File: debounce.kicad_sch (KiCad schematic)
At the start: 3 parts

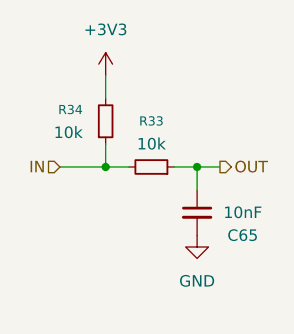
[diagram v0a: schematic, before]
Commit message: Add ultra thin buttons for ABXY
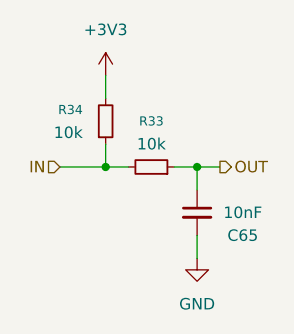
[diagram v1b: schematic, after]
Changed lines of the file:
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@@
+		)
+	)
+	(wire
+		(pts
+			(xy 134.62 111.76) (xy 134.62 109.22)
+		)
+		(stroke
+			(width 0)
+			(type default)
 		)
 	)
@@
 		(instances
 			(project "pedal"
+				(path "/e2443317-b83f-4e66-ac79-3186c6d613f3/08cc2b29-85b9-4aa1-81ca-cf2350ffd532/113d6eb1-d787-4bde-aeea-3b686f86928a"
+					(reference "R45")
+					(unit 1)
+				)
+				(path "/e2443317-b83f-4e66-ac79-3186c6d613f3/08cc2b29-85b9-4aa1-81ca-cf2350ffd532/24d60361-3370-44ad-88df-7f067c4a89f9"
+					(reference "R39")
+					(unit 1)
+				)
+				(path "/e2443317-b83f-4e66-ac79-3186c6d613f3/08cc2b29-85b9-4aa1-81ca-cf2350ffd532/30ff93b2-9c77-4a10-8b70-e2d38cabc23d"
+					(reference "R43")
+					(unit 1)
+				)
+				(path "/e2443317-b83f-4e66-ac79-3186c6d613f3/08cc2b29-85b9-4aa1-81ca-cf2350ffd532/7aa8d5d4-6cdc-47ee-9e8f-839e8028a7b9"
+					(reference "R49")
+					(unit 1)
+				)
+				(path "/e2443317-b83f-4e66-ac79-3186c6d613f3/08cc2b29-85b9-4aa1-81ca-cf2350ffd532/94183d09-d252-4744-b2a1-51f80f1daa54"
+					(reference "R41")
+					(unit 1)
+				)
+				(path "/e2443317-b83f-4e66-ac79-3186c6d613f3/08cc2b29-85b9-4aa1-81ca-cf2350ffd532/9e7ef8af-33b6-41d4-950e-29ca0f5a19bc"
+					(reference "R53")
+					(unit 1)
+				)
+				(path "/e2443317-b83f-4e66-ac79-3186c6d613f3/08cc2b29-85b9-4aa1-81ca-cf2350ffd532/d1f7dbf6-58aa-4f7e-8a98-9b343c116364"
+					(reference "R51")
+					(unit 1)
+				)
+				(path "/e2443317-b83f-4e66-ac79-3186c6d613f3/08cc2b29-85b9-4aa1-81ca-cf2350ffd532/e87d1f28-ed03-40a1-b111-b01404004c38"
+					(reference "R47")
+					(unit 1)
+				)
 				(path "/e2443317-b83f-4e66-ac79-3186c6d613f3/a1bbde72-fd3e-4fef-8e82-ce5db1c82ed5/4c22a4e9-863a-4116-bdb6-63d664a4292f"
 					(reference "R34")
@@
 		(instances
 			(project "pedal"
+				(path "/e2443317-b83f-4e66-ac79-3186c6d613f3/08cc2b29-85b9-4aa1-81ca-cf2350ffd532/113d6eb1-d787-4bde-aeea-3b686f86928a"
+					(reference "C71")
+					(unit 1)
+				)
+				(path "/e2443317-b83f-4e66-ac79-3186c6d613f3/08cc2b29-85b9-4aa1-81ca-cf2350ffd532/24d60361-3370-44ad-88df-7f067c4a89f9"
+					(reference "C68")
+					(unit 1)
+				)
+				(path "/e2443317-b83f-4e66-ac79-3186c6d613f3/08cc2b29-85b9-4aa1-81ca-cf2350ffd532/30ff93b2-9c77-4a10-8b70-e2d38cabc23d"
+					(reference "C70")
+					(unit 1)
+				)
+				(path "/e2443317-b83f-4e66-ac79-3186c6d613f3/08cc2b29-85b9-4aa1-81ca-cf2350ffd532/7aa8d5d4-6cdc-47ee-9e8f-839e8028a7b9"
+					(reference "C73")
+					(unit 1)
+				)
+				(path "/e2443317-b83f-4e66-ac79-3186c6d613f3/08cc2b29-85b9-4aa1-81ca-cf2350ffd532/94183d09-d252-4744-b2a1-51f80f1daa54"
+					(reference "C69")
+					(unit 1)
+				)
+				(path "/e2443317-b83f-4e66-ac79-3186c6d613f3/08cc2b29-85b9-4aa1-81ca-cf2350ffd532/9e7ef8af-33b6-41d4-950e-29ca0f5a19bc"
+					(reference "C75")
+					(unit 1)
+				)
+				(path "/e2443317-b83f-4e66-ac79-3186c6d613f3/08cc2b29-85b9-4aa1-81ca-cf2350ffd532/d1f7dbf6-58aa-4f7e-8a98-9b343c116364"
+					(reference "C74")
+					(unit 1)
+				)
+				(path "/e2443317-b83f-4e66-ac79-3186c6d613f3/08cc2b29-85b9-4aa1-81ca-cf2350ffd532/e87d1f28-ed03-40a1-b111-b01404004c38"
+					(reference "C72")
+					(unit 1)
+				)
 				(path "/e2443317-b83f-4e66-ac79-3186c6d613f3/a1bbde72-fd3e-4fef-8e82-ce5db1c82ed5/4c22a4e9-863a-4116-bdb6-63d664a4292f"
 					(reference "C65")
@@
 	(symbol
 		(lib_id "power:GND")
-		(at 134.62 109.22 0)
+		(at 134.62 111.76 0)
 		(unit 1)
 		(body_style 1)
@@
 		(fields_autoplaced yes)
 		(property "Reference" "#PWR0149"
-			(at 134.62 115.57 0)
+			(at 134.62 118.11 0)
 			(hide yes)
 			(show_name no)
@@
 		)
 		(property "Value" "GND"
-			(at 134.62 114.3 0)
+			(at 134.62 116.84 0)
 			(show_name no)
 			(do_not_autoplace no)
@@
 		)
 		(property "Footprint" ""
-			(at 134.62 109.22 0)
+			(at 134.62 111.76 0)
 			(hide yes)
 			(show_name no)
@@
 		)
 		(property "Datasheet" ""
-			(at 134.62 109.22 0)
+			(at 134.62 111.76 0)
 			(hide yes)
 			(show_name no)
@@
 		)
 		(property "Description" "Power symbol creates a global label with name \"GND\" , ground"
-			(at 134.62 109.22 0)
+			(at 134.62 111.76 0)
 			(hide yes)
 			(show_name no)
@@
 		(instances
 			(project "pedal"
+				(path "/e2443317-b83f-4e66-ac79-3186c6d613f3/08cc2b29-85b9-4aa1-81ca-cf2350ffd532/113d6eb1-d787-4bde-aeea-3b686f86928a"
+					(reference "#PWR0160")
+					(unit 1)
+				)
+				(path "/e2443317-b83f-4e66-ac79-3186c6d613f3/08cc2b29-85b9-4aa1-81ca-cf2350ffd532/24d60361-3370-44ad-88df-7f067c4a89f9"
+					(reference "#PWR0152")
+					(unit 1)
+				)
+				(path "/e2443317-b83f-4e66-ac79-3186c6d613f3/08cc2b29-85b9-4aa1-81ca-cf2350ffd532/30ff93b2-9c77-4a10-8b70-e2d38cabc23d"
+					(reference "#PWR0157")
+					(unit 1)
+				)
+				(path "/e2443317-b83f-4e66-ac79-3186c6d613f3/08cc2b29-85b9-4aa1-81ca-cf2350ffd532/7aa8d5d4-6cdc-47ee-9e8f-839e8028a7b9"
+					(reference "#PWR0166")
+					(unit 1)
+				)
+				(path "/e2443317-b83f-4e66-ac79-3186c6d613f3/08cc2b29-85b9-4aa1-81ca-cf2350ffd532/94183d09-d252-4744-b2a1-51f80f1daa54"
+					(reference "#PWR0155")
+					(unit 1)
+				)
+				(path "/e2443317-b83f-4e66-ac79-3186c6d613f3/08cc2b29-85b9-4aa1-81ca-cf2350ffd532/9e7ef8af-33b6-41d4-950e-29ca0f5a19bc"
+					(reference "#PWR0170")
+					(unit 1)
+				)
+				(path "/e2443317-b83f-4e66-ac79-3186c6d613f3/08cc2b29-85b9-4aa1-81ca-cf2350ffd532/d1f7dbf6-58aa-4f7e-8a98-9b343c116364"
+					(reference "#PWR0168")
+					(unit 1)
+				)
+				(path "/e2443317-b83f-4e66-ac79-3186c6d613f3/08cc2b29-85b9-4aa1-81ca-cf2350ffd532/e87d1f28-ed03-40a1-b111-b01404004c38"
+					(reference "#PWR0163")
+					(unit 1)
+				)
 				(path "/e2443317-b83f-4e66-ac79-3186c6d613f3/a1bbde72-fd3e-4fef-8e82-ce5db1c82ed5/4c22a4e9-863a-4116-bdb6-63d664a4292f"
 					(reference "#PWR0149")
@@
 		(instances
 			(project "pedal"
+				(path "/e2443317-b83f-4e66-ac79-3186c6d613f3/08cc2b29-85b9-4aa1-81ca-cf2350ffd532/113d6eb1-d787-4bde-aeea-3b686f86928a"
+					(reference "#PWR0159")
+					(unit 1)
+				)
+				(path "/e2443317-b83f-4e66-ac79-3186c6d613f3/08cc2b29-85b9-4aa1-81ca-cf2350ffd532/24d60361-3370-44ad-88df-7f067c4a89f9"
+					(reference "#PWR0144")
+					(unit 1)
+				)
+				(path "/e2443317-b83f-4e66-ac79-3186c6d613f3/08cc2b29-85b9-4aa1-81ca-cf2350ffd532/30ff93b2-9c77-4a10-8b70-e2d38cabc23d"
+					(reference "#PWR0148")
+					(unit 1)
+				)
+				(path "/e2443317-b83f-4e66-ac79-3186c6d613f3/08cc2b29-85b9-4aa1-81ca-cf2350ffd532/7aa8d5d4-6cdc-47ee-9e8f-839e8028a7b9"
+					(reference "#PWR0165")
+					(unit 1)
+				)
+				(path "/e2443317-b83f-4e66-ac79-3186c6d613f3/08cc2b29-85b9-4aa1-81ca-cf2350ffd532/94183d09-d252-4744-b2a1-51f80f1daa54"
+					(reference "#PWR0147")
+					(unit 1)
+				)
+				(path "/e2443317-b83f-4e66-ac79-3186c6d613f3/08cc2b29-85b9-4aa1-81ca-cf2350ffd532/9e7ef8af-33b6-41d4-950e-29ca0f5a19bc"
+					(reference "#PWR0169")
+					(unit 1)
+				)
+				(path "/e2443317-b83f-4e66-ac79-3186c6d613f3/08cc2b29-85b9-4aa1-81ca-cf2350ffd532/d1f7dbf6-58aa-4f7e-8a98-9b343c116364"
+					(reference "#PWR0167")
+					(unit 1)
+				)
+				(path "/e2443317-b83f-4e66-ac79-3186c6d613f3/08cc2b29-85b9-4aa1-81ca-cf2350ffd532/e87d1f28-ed03-40a1-b111-b01404004c38"
+					(reference "#PWR0162")
+					(unit 1)
+				)
 				(path "/e2443317-b83f-4e66-ac79-3186c6d613f3/a1bbde72-fd3e-4fef-8e82-ce5db1c82ed5/4c22a4e9-863a-4116-bdb6-63d664a4292f"
 					(reference "#PWR0140")
@@
 		(instances
 			(project "pedal"
+				(path "/e2443317-b83f-4e66-ac79-3186c6d613f3/08cc2b29-85b9-4aa1-81ca-cf2350ffd532/113d6eb1-d787-4bde-aeea-3b686f86928a"
+					(reference "R46")
+					(unit 1)
+				)
+				(path "/e2443317-b83f-4e66-ac79-3186c6d613f3/08cc2b29-85b9-4aa1-81ca-cf2350ffd532/24d60361-3370-44ad-88df-7f067c4a89f9"
+					(reference "R40")
+					(unit 1)
+				)
+				(path "/e2443317-b83f-4e66-ac79-3186c6d613f3/08cc2b29-85b9-4aa1-81ca-cf2350ffd532/30ff93b2-9c77-4a10-8b70-e2d38cabc23d"
+					(reference "R44")
+					(unit 1)
+				)
+				(path "/e2443317-b83f-4e66-ac79-3186c6d613f3/08cc2b29-85b9-4aa1-81ca-cf2350ffd532/7aa8d5d4-6cdc-47ee-9e8f-839e8028a7b9"
+					(reference "R50")
+					(unit 1)
+				)
+				(path "/e2443317-b83f-4e66-ac79-3186c6d613f3/08cc2b29-85b9-4aa1-81ca-cf2350ffd532/94183d09-d252-4744-b2a1-51f80f1daa54"
+					(reference "R42")
+					(unit 1)
+				)
+				(path "/e2443317-b83f-4e66-ac79-3186c6d613f3/08cc2b29-85b9-4aa1-81ca-cf2350ffd532/9e7ef8af-33b6-41d4-950e-29ca0f5a19bc"
+					(reference "R54")
+					(unit 1)
+				)
+				(path "/e2443317-b83f-4e66-ac79-3186c6d613f3/08cc2b29-85b9-4aa1-81ca-cf2350ffd532/d1f7dbf6-58aa-4f7e-8a98-9b343c116364"
+					(reference "R52")
+					(unit 1)
+				)
+				(path "/e2443317-b83f-4e66-ac79-3186c6d613f3/08cc2b29-85b9-4aa1-81ca-cf2350ffd532/e87d1f28-ed03-40a1-b111-b01404004c38"
+					(reference "R48")
+					(unit 1)
+				)
 				(path "/e2443317-b83f-4e66-ac79-3186c6d613f3/a1bbde72-fd3e-4fef-8e82-ce5db1c82ed5/4c22a4e9-863a-4116-bdb6-63d664a4292f"
 					(reference "R33")
